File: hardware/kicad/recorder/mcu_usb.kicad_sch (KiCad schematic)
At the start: 11 parts, among them J1 UART0, J2 USB_C_16P, U1 ESP32-S3-MINI-1U-N8, U7 USBLC6-2SC6

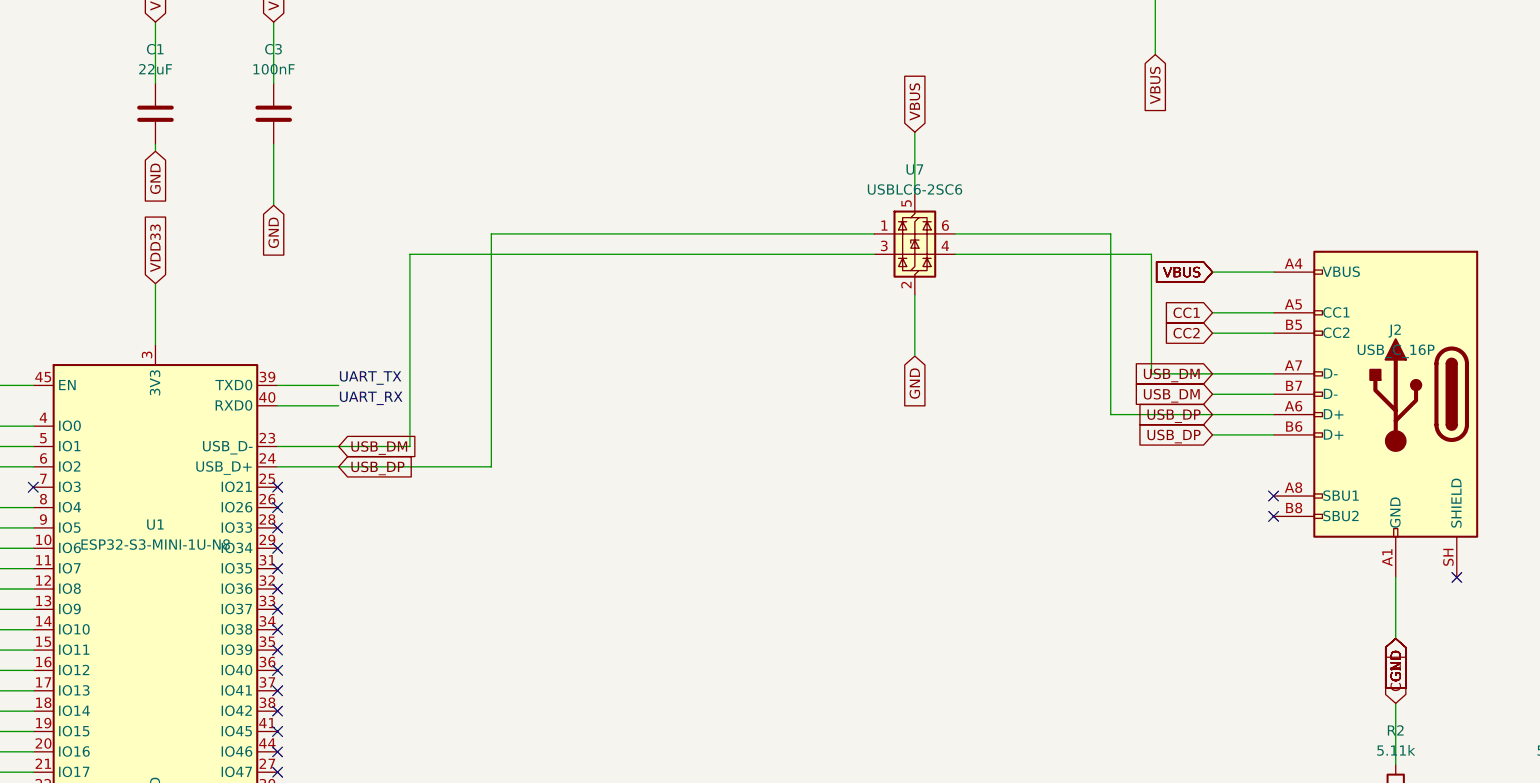
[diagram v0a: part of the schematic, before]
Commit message: Route the recorder board and make the fab package match it
The board had planes but no signals. It now carries 694 traces and 193
vias from freerouting, driven headless through Specctra DSN/SES, with the
USB pair, the ES8311 fanout and the analog island hand-routed first and
locked so rip-up cannot cut them.

kicad-cli pcb drc now reports zero violations at every severity and zero
unconnected items.

Two things that would have scrapped a real order:

- check_gates.py re-exported Gerbers but left the drill file, the
  pick-and-place CSV and recorder-jlc.zip at whatever date they were
  committed with. The drill file on disk predated routing and had no
  0.3 mm tool, so the package described a board with none of its vias
  drilled. The whole package is now written in one pass from one board
  file, gated on a real kicad-cli pcb drc run.
- check_placement.py trusted BOX2I.Merge()'s return value, which is an
  unrelated proxy in the SWIG bindings, and measured courtyards from
  GetCourtyard(), which is inflated past the drawn outline. That invented
  four off-board mounting holes and six overlaps. It reads the drawn
  shapes now, and check_gates runs it when pcbnew is importable.

Silkscreen designators are shrunk to the 0.8 mm / 0.15 mm fab floor and
re-seated on a full angular sweep, clearing all 29 silk warnings.

Co-authored-by: zeeman <zeeman-effect@users.noreply.github.com>
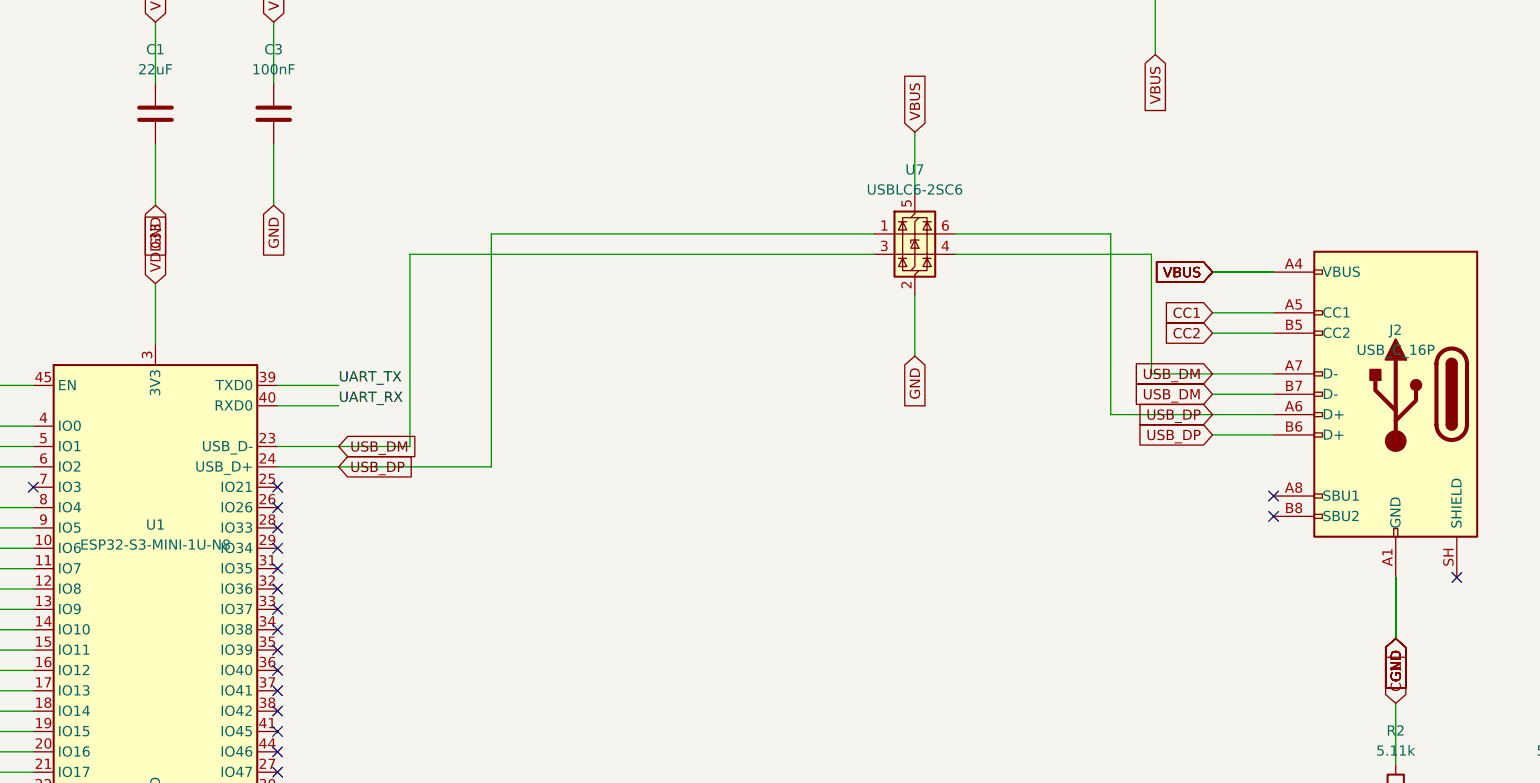
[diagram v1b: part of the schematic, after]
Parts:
- U1: footprint RF_Module:ESP32-S3-MINI-1 -> PSV:ESP32-S3-MINI-1U

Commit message: Route USB as a real pair and ground the USB-C shell
The autorouter sent D+ on a 16.6 mm diagonal across B.Cu. B.Cu is the face
that lies against the phone and is otherwise a solid GND pour, so that
slotted the shield and ran a USB line straight at the handset.

U1's USB pads sit on the module's top row, the far side of a 15.9 mm
module from J2, and the castellations leave 0.05 mm between pads, so the
pair cannot cross the footprint. It now goes up the 3.3 mm channel
between J1 and U1 in two lanes 0.4 mm apart. Both nets already surface
west of J2 on their own link, so extending those links west drops each
into its lane with no crossing anywhere on the board. U7 hangs off the
lanes as a short stub instead of sitting in series, which costs nothing:
it is a shunt TVS and clamps to GND wherever it is tapped.

D+ 45.8 mm, D- 44.2 mm end to end. Skew is down from 6.9 mm to 1.65 mm
and B.Cu on the pair from 30 mm to 4.4 mm.

J2's shell was a no-connect, which left the four retention tabs on a
placeholder net that DRC wanted joined to each other and no amount of
re-routing could close. It is GND now, which is what a connector shell
wants anyway.

generate_recorder.py assumed the Windows KiCad install path, so it only
ran on one laptop; it searches the usual locations now.

Co-authored-by: zeeman <zeeman-effect@users.noreply.github.com>
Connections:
- net GND: now also J2.SH (SHIELD)
- no-connect marks 20 -> 19
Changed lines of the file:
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@@
+		(effects (font (size 1.27 1.27)) (justify right))
+	)
+	(wire
+		(pts (xy 257.62 112.86) (xy 257.62 120.48))
+		(stroke (width 0) (type default))
+	)
+	(global_label "GND"
+		(shape input)
+		(at 257.62 120.48 270)
 		(effects (font (size 1.27 1.27)) (justify right))
 	)
@@
 		(at 234.76 105.24)
 	)
-	(no_connect
-		(at 257.62 112.86)
-	)
 	(symbol
